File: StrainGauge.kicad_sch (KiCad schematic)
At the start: 23 parts, among them J1 Conn_01x04, J2 Conn_01x04, U1 INA333xxDGK, U2 REF2025

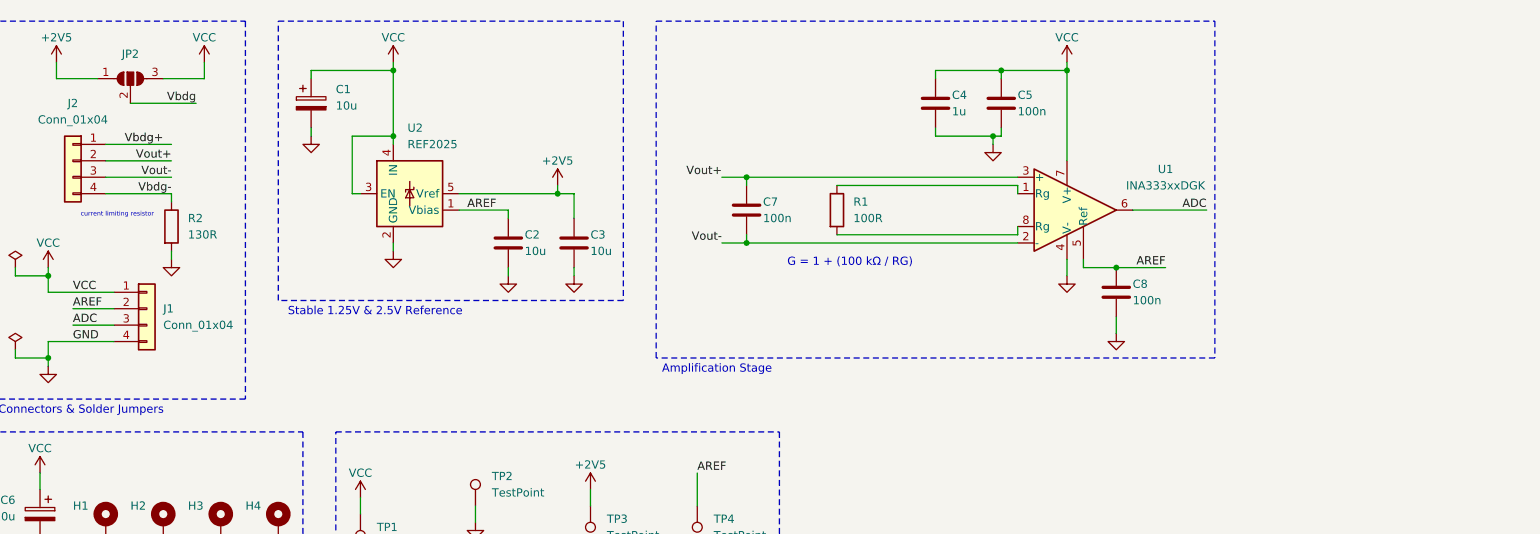
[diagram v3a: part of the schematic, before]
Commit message: added ref-voltage output buffer
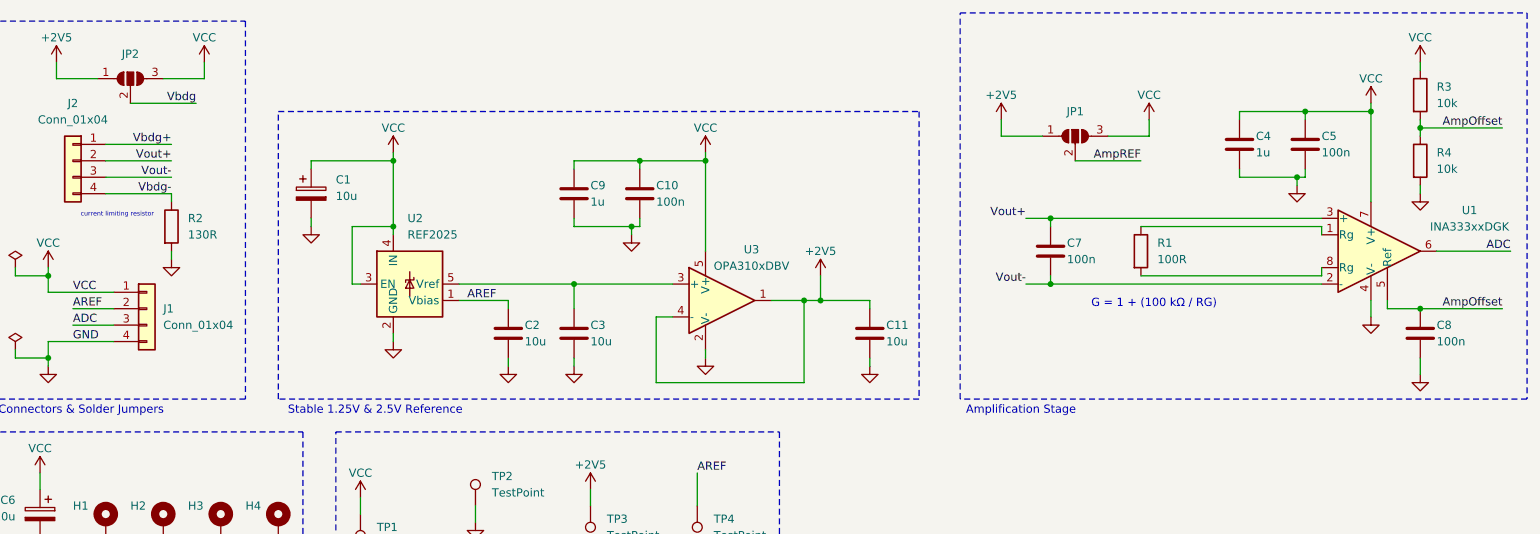
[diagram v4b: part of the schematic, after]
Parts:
- added C10: 100n, symbol Device:C
- added C11: 10u, symbol Device:C
- added C9: 1u, symbol Device:C
- added JP1: SolderJumper_3_Open, symbol Jumper:SolderJumper_3_Open
- added R3, R4: 10k, symbol Device:R
- added U3: OPA310xDBV, Package_TO_SOT_SMD:SOT-23-5, symbol Amplifier_Operational:OPA310xDBV
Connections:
- net +2V5: now also C11.1, JP1.1 (A), U3.1, U3.4 (-); no longer C3.1, U2.5 (Vref)
- net AREF: no longer C8.1, U1.5 (Ref)
- net GND: now also C10.2, C11.2, C9.2, R4.2, U3.2 (V-)
- net VCC: now also C10.1, C9.1, JP1.3 (B), R3.1, U3.5 (V+)
- new net: C3.1, U2.5 (Vref), U3.3 (+)
- new net AmpOffset: C8.1, R3.2, R4.1, U1.5 (Ref)
- new net AmpREF: JP1.2 (C)
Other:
- moved on the sheet: C1, C2, C3, C4, C5, C7, C8, R1, U1, U2

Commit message: minor changes, need to add potentiometer next
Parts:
- removed R2: 130R, symbol Device:R
- renumbered R3 to R2, R4 to R3
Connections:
- net Vbdg is gone; now on net Vbdg+: JP2.2 (C)
- net Vbdg- is gone; now on net GND: J2.4 (Pin_4)
- net AmpOffset: now also JP1.3 (B); no longer C8.1, U1.5 (Ref)
- net AmpREF: now also C8.1, U1.5 (Ref)
- net VCC: no longer JP1.3 (B)
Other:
- note removed: "current limiting resistor"
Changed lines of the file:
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@@
 	(wire
 		(pts
-			(xy 212.09 44.45) (xy 212.09 46.99)
-		)
-		(stroke
-			(width 0)
-			(type default)
-		)
-	)
-	(wire
-		(pts
 			(xy 95.25 49.53) (xy 95.25 50.8)
 		)
@@
 	(wire
 		(pts
-			(xy 60.96 66.04) (xy 60.96 64.77)
-		)
-		(stroke
-			(width 0)
-			(type default)
-		)
-	)
-	(wire
-		(pts
 			(xy 90.17 102.87) (xy 90.17 105.41)
 		)
@@
 	(wire
 		(pts
-			(xy 205.74 46.99) (xy 212.09 46.99)
+			(xy 205.74 46.99) (xy 218.44 46.99)
 		)
 		(stroke
@@
 	(wire
 		(pts
-			(xy 54.61 41.91) (xy 64.77 41.91)
+			(xy 54.61 41.91) (xy 63.5 41.91)
 		)
 		(stroke
@@
 		)
 	)
-	(text "current limiting resistor"
-		(exclude_from_sim no)
-		(at 52.578 59.182 0)
-		(effects
-			(font
-				(size 0.7 0.7)
-			)
-		)
-	)
 	(text "The current limiting resistor is a big liability in the voltage sensing\nability of the bridge. The following circuit instead uses a \nbuffer + transistor setup to source current into the bridge without being\nlimited by the small output current of the stable voltage reference. This\ncan be used as a starting point for a robust voltage source with good\ncurrent sourcing capability."
 		(exclude_from_sim no)
@@
 		)
 	)
-	(label "AmpOffset"
+	(label "AmpREF"
 		(at 266.7 73.66 180)
 		(fields_autoplaced yes)
@@
 		)
 	)
+	(label "AmpOffset"
+		(at 218.44 46.99 180)
+		(fields_autoplaced yes)
+		(effects
+			(font
+				(size 1.27 1.27)
+			)
+			(justify right bottom)
+		)
+	)
 	(label "Vout-"
 		(at 60.96 53.34 180)
@@
 		)
 	)
-	(label "Vbdg"
-		(at 64.77 41.91 180)
+	(label "Vbdg+"
+		(at 63.5 41.91 180)
 		(fields_autoplaced yes)
 		(effects
@@
 	(symbol
 		(lib_id "power:GND")
-		(at 60.96 66.04 0)
+		(at 60.96 57.15 0)
 		(unit 1)
 		(exclude_from_sim no)
@@
 		(fields_autoplaced yes)
 		(property "Reference" "#PWR03"
-			(at 60.96 72.39 0)
+			(at 60.96 63.5 0)
 			(effects
 				(font
@@
 		)
 		(property "Value" "GND"
-			(at 60.96 71.12 0)
+			(at 60.96 62.23 0)
 			(effects
 				(font
@@
 		)
 		(property "Footprint" ""
-			(at 60.96 66.04 0)
+			(at 60.96 57.15 0)
 			(effects
 				(font
@@
 		)
 		(property "Datasheet" ""
-			(at 60.96 66.04 0)
+			(at 60.96 57.15 0)
 			(effects
 				(font
@@
 		)
 		(property "Description" "Power symbol creates a global label with name \"GND\" , ground"
-			(at 60.96 66.04 0)
+			(at 60.96 57.15 0)
 			(effects
 				(font
@@
 	)
 	(symbol
-		(lib_id "Device:R")
-		(at 60.96 60.96 0)
-		(unit 1)
-		(exclude_from_sim no)
-		(in_bom yes)
-		(on_board yes)
-		(dnp no)
-		(fields_autoplaced yes)
-		(property "Reference" "R2"
-			(at 63.5 59.6899 0)
-			(effects
-				(font
-					(size 1.27 1.27)
-				)
-				(justify left)
-			)
-		)
-		(property "Value" "130R"
-			(at 63.5 62.2299 0)
-			(effects
-				(font
-					(size 1.27 1.27)
-				)
-				(justify left)
-			)
-		)
-		(property "Footprint" ""
-			(at 59.182 60.96 90)
-			(effects
-				(font
-					(size 1.27 1.27)
-				)
-				(hide yes)
-			)
-		)
-		(property "Datasheet" "~"
-			(at 60.96 60.96 0)
-			(effects
-				(font
-					(size 1.27 1.27)
-				)
-				(hide yes)
-			)
-		)
-		(property "Description" "Resistor"
-			(at 60.96 60.96 0)
-			(effects
-				(font
-					(size 1.27 1.27)
-				)
-				(hide yes)
-			)
-		)
-		(pin "1"
-		)
-		(pin "2"
-		)
-		(instances
-			(project ""
-				(path "/1c58ffeb-c530-4561-bcfa-51e04fb88036"
-					(reference "R2")
-					(unit 1)
-				)
-			)
-		)
-	)
-	(symbol
 		(lib_id "Connector:TestPoint")
 		(at 90.17 105.41 180)
@@
 	)
 	(symbol
-		(lib_id "power:VCC")
-		(at 212.09 44.45 0)
-		(unit 1)
-		(exclude_from_sim no)
-		(in_bom yes)
-		(on_board yes)
-		(dnp no)
-		(property "Reference" "#PWR025"
-			(at 212.09 48.26 0)
-			(effects
-				(font
-					(size 1.27 1.27)
-				)
-				(hide yes)
-			)
-		)
-		(property "Value" "VCC"
-			(at 212.09 40.64 0)
-			(effects
-				(font
-					(size 1.27 1.27)
-				)
-			)
-		)
-		(property "Footprint" ""
-			(at 212.09 44.45 0)
-			(effects
-				(font
-					(size 1.27 1.27)
-				)
-				(hide yes)
-			)
-		)
-		(property "Datasheet" ""
-			(at 212.09 44.45 0)
-			(effects
-				(font
-					(size 1.27 1.27)
-				)
-				(hide yes)
-			)
-		)
-		(property "Description" "Power symbol creates a global label with name \"VCC\""
-			(at 212.09 44.45 0)
-			(effects
-				(font
-					(size 1.27 1.27)
-				)
-				(hide yes)
-			)
-		)
-		(pin "1"
-		)
-		(instances
-			(project "StrainGauge"
-				(path "/1c58ffeb-c530-4561-bcfa-51e04fb88036"
-					(reference "#PWR025")
-					(unit 1)
-				)
-			)
-		)
-	)
-	(symbol
 		(lib_id "Amplifier_Instrumentation:INA333xxDGK")
 		(at 246.38 64.77 0)
@@
 		(dnp no)
 		(fields_autoplaced yes)
-		(property "Reference" "R3"
+		(property "Reference" "R2"
 			(at 256.54 39.3699 0)
 			(effects
@@
 			(project ""
 				(path "/1c58ffeb-c530-4561-bcfa-51e04fb88036"
-					(reference "R3")
+					(reference "R2")
 					(unit 1)
 				)
@@
 		(dnp no)
 		(fields_autoplaced yes)
-		(property "Reference" "R4"
+		(property "Reference" "R3"
 			(at 256.54 49.5299 0)
 			(effects
@@
 			(project "StrainGauge"
 				(path "/1c58ffeb-c530-4561-bcfa-51e04fb88036"
-					(reference "R4")
+					(reference "R3")
 					(unit 1)
 				)

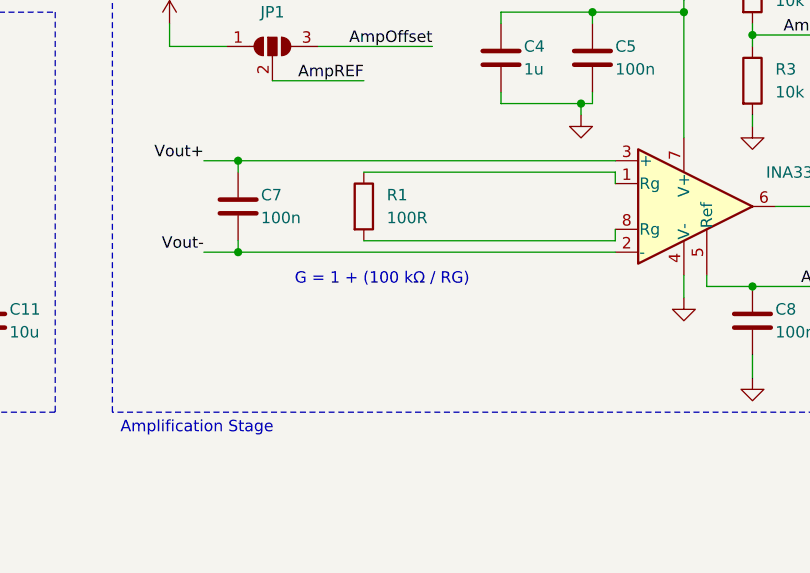
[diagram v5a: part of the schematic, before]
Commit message: added potentiometer
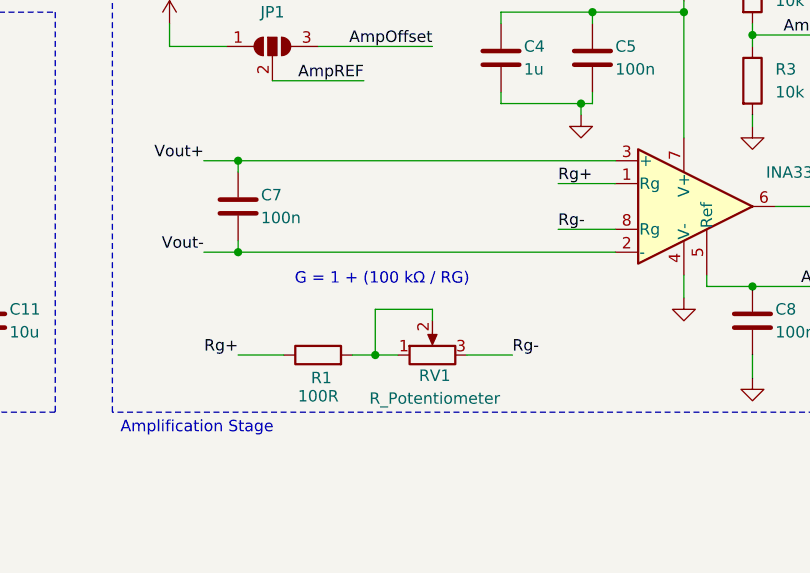
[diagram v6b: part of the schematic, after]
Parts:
- added RV1: R_Potentiometer, symbol Device:R_Potentiometer
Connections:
- net Rg+: now reaches R1.1, U1.1 (Rg)
- net at R1.2: now also RV1.1, RV1.2; no longer U1.8 (Rg)
- new net Rg-: RV1.3, U1.8 (Rg)
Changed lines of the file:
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@@
 	)
 	(junction
+		(at 212.09 81.28)
+		(diameter 0)
+		(color 0 0 0 0)
+	)
+	(junction
 		(at 236.22 43.18)
 		(diameter 0)
@@
 	(wire
 		(pts
-			(xy 238.76 60.96) (xy 238.76 62.23)
-		)
-		(stroke
-			(width 0)
-			(type default)
-		)
-	)
-	(wire
-		(pts
 			(xy 41.91 78.74) (xy 52.07 78.74)
 		)
@@
 	(wire
 		(pts
+			(xy 201.93 81.28) (xy 196.85 81.28)
+		)
+		(stroke
+			(width 0)
+			(type default)
+		)
+	)
+	(wire
+		(pts
 			(xy 132.08 60.96) (xy 133.35 60.96)
 		)
@@
 	(wire
 		(pts
-			(xy 238.76 68.58) (xy 238.76 67.31)
+			(xy 212.09 81.28) (xy 214.63 81.28)
 		)
 		(stroke
@@
 	(wire
 		(pts
+			(xy 212.09 76.2) (xy 212.09 81.28)
+		)
+		(stroke
+			(width 0)
+			(type default)
+		)
+	)
+	(wire
+		(pts
 			(xy 95.25 49.53) (xy 95.25 50.8)
 		)
@@
 	(wire
 		(pts
+			(xy 232.41 67.31) (xy 238.76 67.31)
+		)
+		(stroke
+			(width 0)
+			(type default)
+		)
+	)
+	(wire
+		(pts
+			(xy 209.55 81.28) (xy 212.09 81.28)
+		)
+		(stroke
+			(width 0)
+			(type default)
+		)
+	)
+	(wire
+		(pts
 			(xy 254 73.66) (xy 248.92 73.66)
 		)
@@
 	(wire
 		(pts
-			(xy 210.82 60.96) (xy 238.76 60.96)
+			(xy 227.33 81.28) (xy 222.25 81.28)
 		)
 		(stroke
@@
 	(wire
 		(pts
+			(xy 232.41 62.23) (xy 238.76 62.23)
+		)
+		(stroke
+			(width 0)
+			(type default)
+		)
+	)
+	(wire
+		(pts
 			(xy 123.19 59.69) (xy 123.19 60.96)
 		)
@@
 	(wire
 		(pts
-			(xy 210.82 68.58) (xy 238.76 68.58)
+			(xy 133.35 50.8) (xy 133.35 52.07)
 		)
 		(stroke
@@
 	(wire
 		(pts
-			(xy 133.35 50.8) (xy 133.35 52.07)
+			(xy 196.85 68.58) (xy 196.85 69.85)
 		)
 		(stroke
@@
 	(wire
 		(pts
-			(xy 196.85 68.58) (xy 196.85 69.85)
+			(xy 218.44 76.2) (xy 212.09 76.2)
 		)
 		(stroke
@@
 	(wire
 		(pts
+			(xy 218.44 77.47) (xy 218.44 76.2)
+		)
+		(stroke
+			(width 0)
+			(type default)
+		)
+	)
+	(wire
+		(pts
 			(xy 95.25 60.96) (xy 88.9 60.96)
 		)
@@
 		)
 	)
+	(label "Rg+"
+		(at 196.85 81.28 180)
+		(fields_autoplaced yes)
+		(effects
+			(font
+				(size 1.27 1.27)
+			)
+			(justify right bottom)
+		)
+	)
 	(label "AmpREF"
 		(at 210.82 50.8 180)
@@
 		)
 	)
+	(label "Rg+"
+		(at 232.41 62.23 0)
+		(fields_autoplaced yes)
+		(effects
+			(font
+				(size 1.27 1.27)
+			)
+			(justify left bottom)
+		)
+	)
+	(label "Rg-"
+		(at 227.33 81.28 0)
+		(fields_autoplaced yes)
+		(effects
+			(font
+				(size 1.27 1.27)
+			)
+			(justify left bottom)
+		)
+	)
 	(label "Vout-"
 		(at 193.04 69.85 180)
@@
 		)
 	)
+	(label "Rg-"
+		(at 232.41 67.31 0)
+		(fields_autoplaced yes)
+		(effects
+			(font
+				(size 1.27 1.27)
+			)
+			(justify left bottom)
+		)
+	)
 	(symbol
 		(lib_id "power:VCC")
@@
 	)
 	(symbol
-		(lib_id "Device:R")
-		(at 210.82 64.77 0)
-		(unit 1)
-		(exclude_from_sim no)
-		(in_bom yes)
-		(on_board yes)
-		(dnp no)
-		(property "Reference" "R1"
-			(at 213.36 63.5 0)
-			(effects
-				(font
-					(size 1.27 1.27)
-				)
-				(justify left)
-			)
-		)
-		(property "Value" "100R"
-			(at 213.36 66.04 0)
-			(effects
-				(font
-					(size 1.27 1.27)
-				)
-				(justify left)
-			)
-		)
-		(property "Footprint" ""
-			(at 209.042 64.77 90)
-			(effects
-				(font
-					(size 1.27 1.27)
-				)
-				(hide yes)
-			)
-		)
-		(property "Datasheet" "~"
-			(at 210.82 64.77 0)
-			(effects
-				(font
-					(size 1.27 1.27)
-				)
-				(hide yes)
-			)
-		)
-		(property "Description" "Resistor"
-			(at 210.82 64.77 0)
-			(effects
-				(font
-					(size 1.27 1.27)
-				)
-				(hide yes)
-			)
-		)
-		(pin "1"
-		)
-		(pin "2"
-		)
-		(instances
-			(project ""
-				(path "/1c58ffeb-c530-4561-bcfa-51e04fb88036"
-					(reference "R1")
-					(unit 1)
-				)
-			)
-		)
-	)
-	(symbol
 		(lib_id "power:VCC")
 		(at 40.64 99.06 0)
@@
 	)
 	(symbol
+		(lib_id "Device:R_Potentiometer")
+		(at 218.44 81.28 90)
+		(unit 1)
+		(exclude_from_sim no)
+		(in_bom yes)
+		(on_board yes)
+		(dnp no)
+		(property "Reference" "RV1"
+			(at 218.694 83.566 90)
+			(effects
+				(font
+					(size 1.27 1.27)
+				)
+			)
+		)
+		(property "Value" "R_Potentiometer"
+			(at 218.694 86.106 90)
+			(effects
+				(font
+					(size 1.27 1.27)
+				)
+			)
+		)
+		(property "Footprint" ""
+			(at 218.44 81.28 0)
+			(effects
+				(font
+					(size 1.27 1.27)
+				)
+				(hide yes)
+			)
+		)
+		(property "Datasheet" "~"
+			(at 218.44 81.28 0)
+			(effects
+				(font
+					(size 1.27 1.27)
+				)
+				(hide yes)
+			)
+		)
+		(property "Description" "Potentiometer"
+			(at 218.44 81.28 0)
+			(effects
+				(font
+					(size 1.27 1.27)
+				)
+				(hide yes)
+			)
+		)
+		(pin "1"
+		)
+		(pin "2"
+		)
+		(pin "3"
+		)
+		(instances
+			(project ""
+				(path "/1c58ffeb-c530-4561-bcfa-51e04fb88036"
+					(reference "RV1")
+					(unit 1)
+				)
+			)
+		)
+	)
+	(symbol
 		(lib_id "power:GND")
 		(at 168.91 82.55 0)
@@
 					(unit 1)
 				)
+			)
+		)
+	)
+	(symbol
+		(lib_id "Device:R")
+		(at 205.74 81.28 90)
+		(unit 1)
+		(exclude_from_sim no)
+		(in_bom yes)
+		(on_board yes)
+		(dnp no)
+		(property "Reference" "R1"
+			(at 207.264 83.82 90)
+			(effects
+				(font
+					(size 1.27 1.27)
+				)
+				(justify left)
+			)
+		)
+		(property "Value" "100R"
+			(at 208.026 85.852 90)
+			(effects
+				(font
+					(size 1.27 1.27)
+				)
+				(justify left)
+			)
+		)
+		(property "Footprint" ""
+			(at 205.74 83.058 90)
+			(effects
+				(font
+					(size 1.27 1.27)
+				)
+				(hide yes)
+			)
+		)
+		(property "Datasheet" "~"
+			(at 205.74 81.28 0)
+			(effects
+				(font
+					(size 1.27 1.27)
+				)
+				(hide yes)
+			)
+		)
+		(property "Description" "Resistor"
+			(at 205.74 81.28 0)
+			(effects
+				(font
+					(size 1.27 1.27)
+				)
+				(hide yes)
+			)
+		)
+		(pin "1"
+		)
+		(pin "2"
+		)
+		(instances
+			(project "StrainGauge"
+				(path "/1c58ffeb-c530-4561-bcfa-51e04fb88036"
+					(reference "R1")
+					(unit 1)
+				)

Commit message: small fixes
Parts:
- added R4: 130R, symbol Device:R
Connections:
- net GND: now also R4.1, R4.2
- no-connect marks 0 -> 1
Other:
- note added: "Choose whether to excite bridge with stable 2.5V or battery"
- note added: "Choose whether to use stable 1.25V as OpAmp ref or voltage divider from battery"
- moved on the sheet: C8

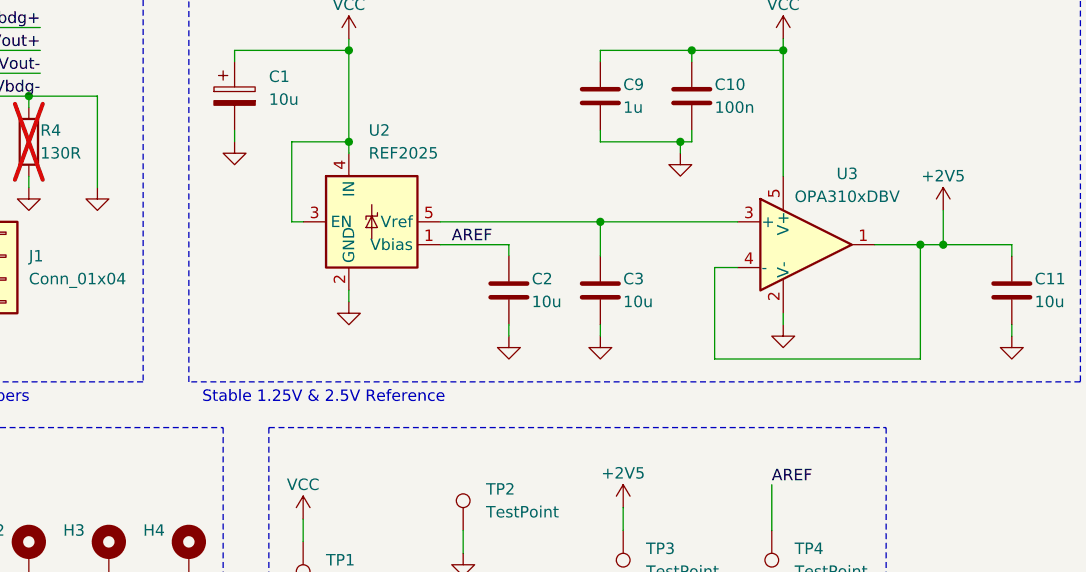
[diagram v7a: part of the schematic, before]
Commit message: added footprints and 3D models
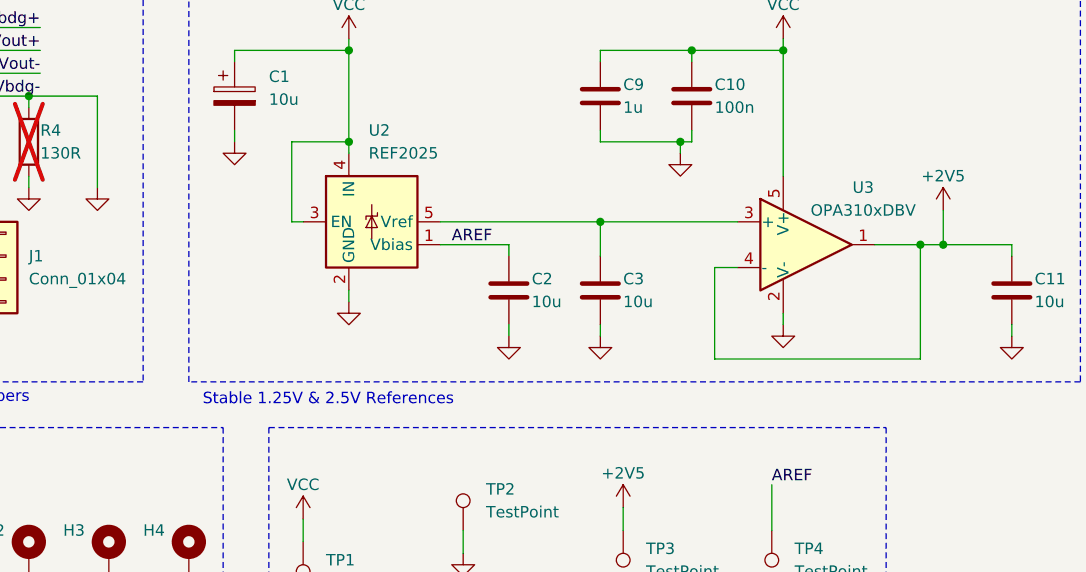
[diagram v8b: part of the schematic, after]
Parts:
- C1, C11, C2, C3, C6: footprint (none) -> Capacitor_SMD:C_0805_2012Metric
- C10, C5, C7, C8: footprint (none) -> Capacitor_SMD:C_0402_1005Metric
- C4, C9: footprint (none) -> Capacitor_SMD:C_0603_1608Metric
- H1, H2, H3, H4: footprint (none) -> MountingHole:MountingHole_2.2mm_M2_Pad_Via
- J1: footprint (none) -> Connector_PinHeader_2.54mm:PinHeader_1x04_P2.54mm_Vertical
- J2: footprint (none) -> CLIK-Mate 502585:5025850470
- JP1, JP2: footprint (none) -> Jumper:SolderJumper-3_P1.3mm_Open_RoundedPad1.0x1.5mm
- R1, R2, R3, R4: footprint (none) -> Resistor_SMD:R_0402_1005Metric
- RV1: footprint (none) -> PV36W103C01B00:TRIM_PV36W103C01B00
- TP1, TP2, TP3, TP4: footprint (none) -> TestPoint:TestPoint_Plated_Hole_D2.0mm
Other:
- note added: "Stable 1.25V & 2.5V References"
- note removed: "Stable 1.25V & 2.5V Reference"
